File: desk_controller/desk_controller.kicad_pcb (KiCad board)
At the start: 2 copper layers, 92.8 x 125.7 mm, 56 parts, among them J2 UART_passthrough, J3 SWD_header, SW2 STRIP_PWR_SW, SW3 PC_PWR_RST_SW, SW4 OS_SW, U1 BD95831MUV, U2 PC817, U3 AP2112K-3.3, U4 TRS3243ECRHBR, U5 ISO7341FC, U6 STM32F030K6T6, U7 PC817

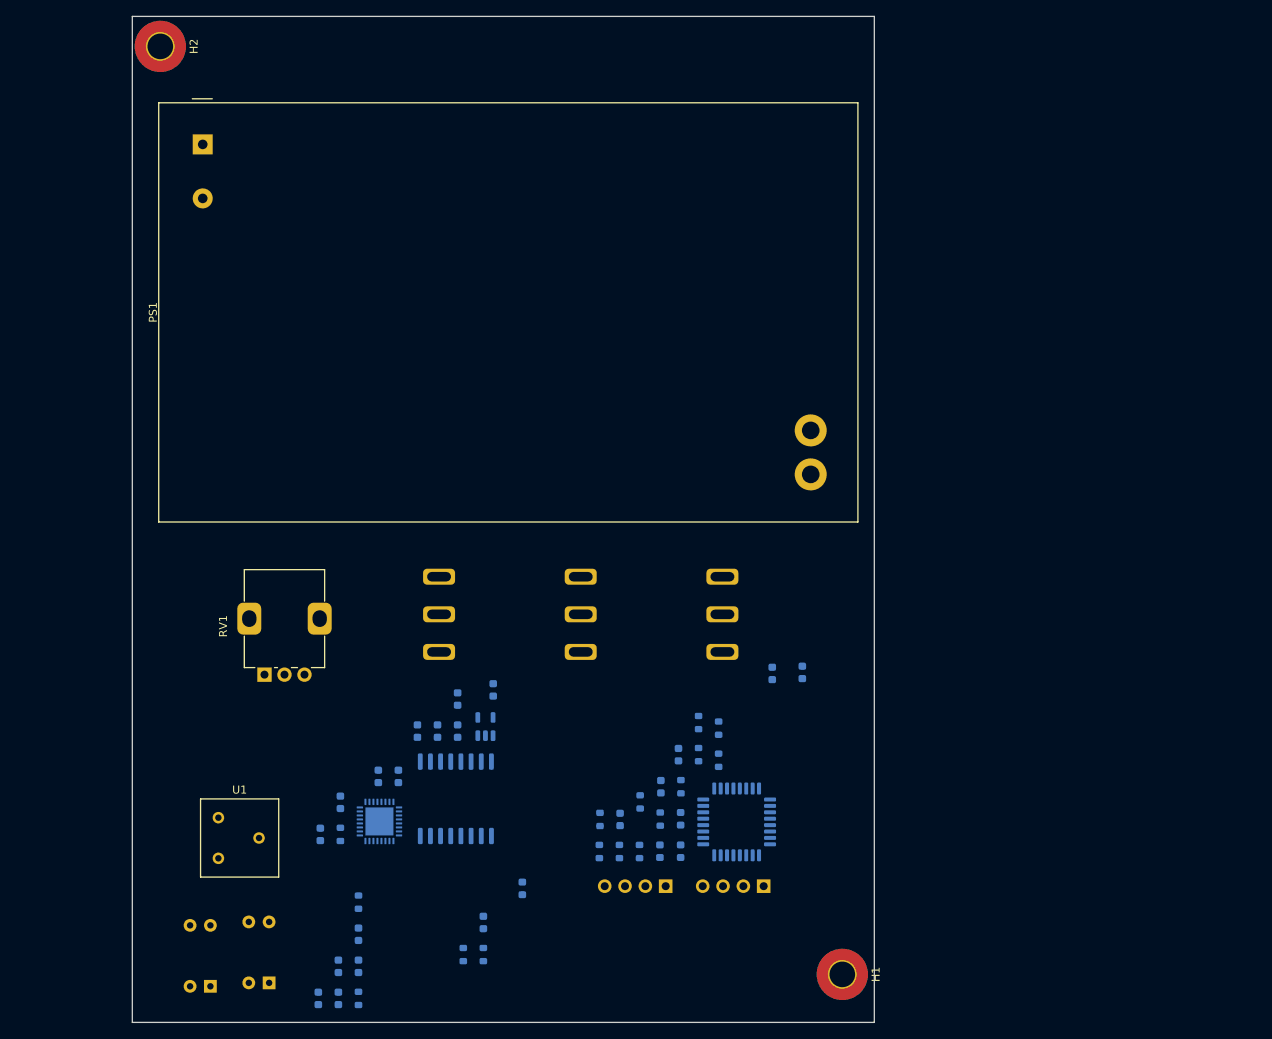
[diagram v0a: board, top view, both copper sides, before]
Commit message: Removed acdc brick
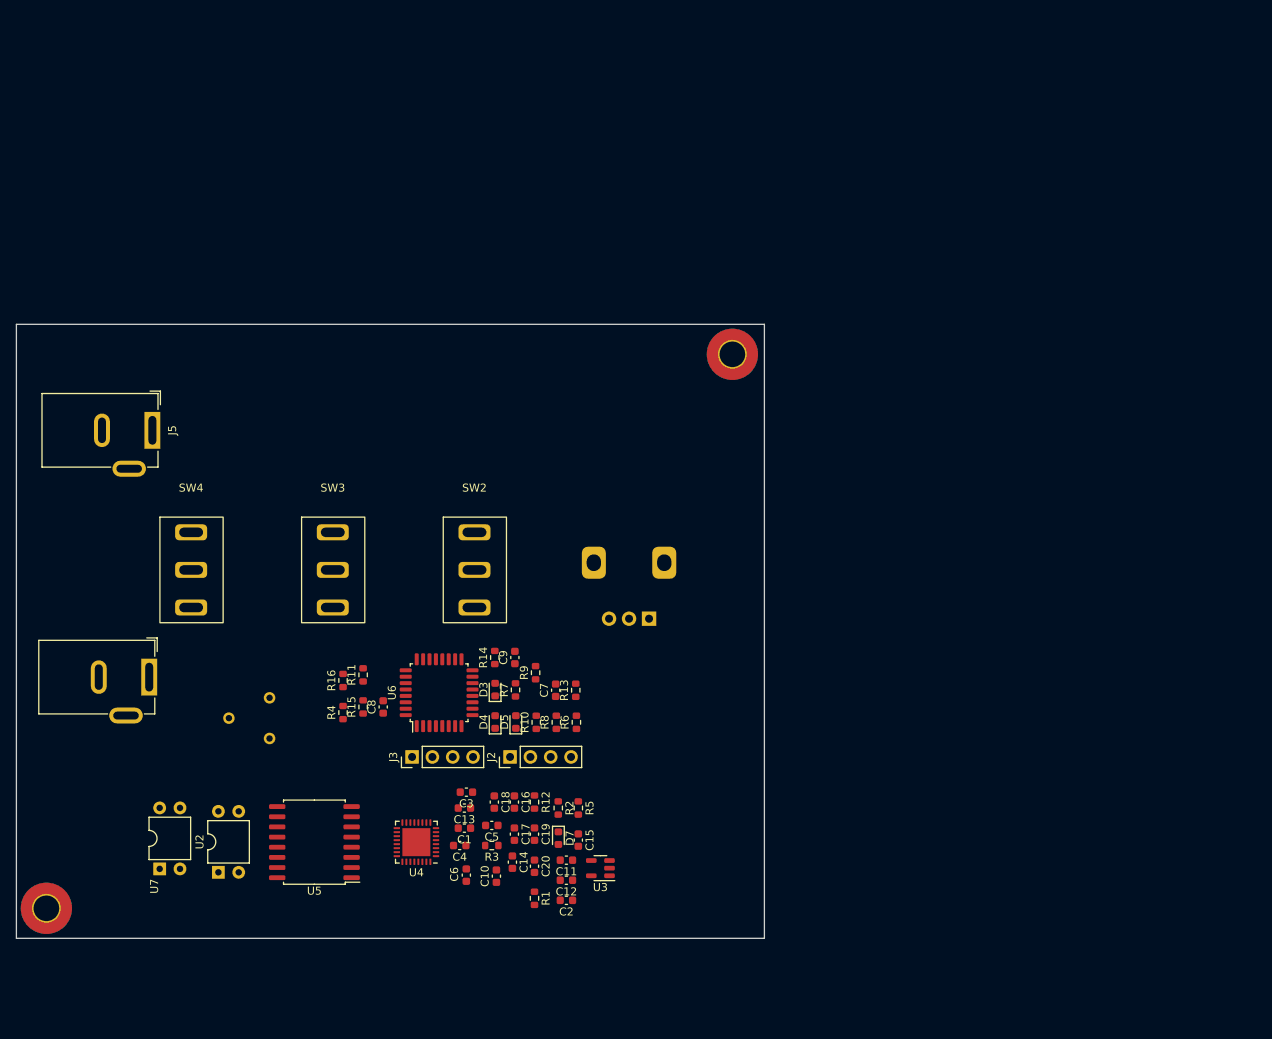
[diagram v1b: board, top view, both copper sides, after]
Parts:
- removed PS1: IRM-60-12, Converter_ACDC:Converter_ACDC_MeanWell_IRM-60-xx_THT
- added J4: Barrel_Jack_MountingPin, Connector_BarrelJack:BarrelJack_GCT_DCJ200-10-A_Horizontal, F.Cu at (105.8, 87.8)
- added J5: Barrel_Jack_MountingPin, Connector_BarrelJack:BarrelJack_GCT_DCJ200-10-A_Horizontal, F.Cu at (106.2, 57.0)
- C1, C10, C11, C12, C13, C14, C15, C16, C17, C18, C19, C2, C20, C3, C4, C5, C6, C7, C8, C9, D3, D4, D5, D7, J2, J3, R1, R10, R11, R12, R13, R14, R15, R16, R2, R3, R4, R5, R6, R7, R8, R9, SW2, SW3, SW4, U2, U3, U4, U5, U6, U7: moved to F.Cu
- RV1, U1: moved to B.Cu
- moved H1 99.8 mm to (93.0, 116.8)
- moved H2 81.2 mm to (178.8, 47.5)
- moved SW4 66.6 mm to (111.1, 74.5), turned to 0 degrees
- moved C6 49.1 mm to (145.5, 112.6)
- moved RV1 48.6 mm to (168.3, 80.5)
- moved R16 47.3 mm to (130.1, 88.3)
- moved R4 47.3 mm to (130.1, 92.3)
- moved J3 46.8 mm to (138.7, 97.8)
- moved C10 42.8 mm to (149.2, 112.7)
- moved R15 42.4 mm to (132.6, 91.6)
- moved R11 42.4 mm to (132.6, 87.6)
- moved U6 40.5 mm to (142.1, 89.8)
- moved C8 37.4 mm to (135.1, 91.6)
- moved C18 33.0 mm to (149.0, 103.5), turned to -90 degrees
- moved C16 33.0 mm to (151.5, 103.5), turned to -90 degrees
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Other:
- board size 92.8 x 125.7 mm -> 93.5 x 76.8 mm

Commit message: Much progress in sch and brd
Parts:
- removed C20: 22u, Capacitor_SMD:C_0603_1608Metric
- removed J2: UART_passthrough, Connector_PinHeader_2.54mm:PinHeader_1x04_P2.54mm_Vertical
- removed R12: 3k3, Resistor_SMD:R_0603_1608Metric
- removed R16: 1k, Resistor_SMD:R_0603_1608Metric
- removed RV1: STRIP_BRIGTH, Potentiometer_THT:Potentiometer_Alps_RK09K_Single_Vertical
- added D1: D_Schottky, Diode_SMD:D_0805_2012Metric, B.Cu at (238.9, 75.5)
- added D2: D_Schottky, Diode_SMD:D_0805_2012Metric, B.Cu at (238.9, 77.6)
- added D6: RED, LED_SMD:LED_0603_1608Metric, B.Cu at (199.2, 86.8)
- added J1: RJ45, Connector_RJ:RJ45_Ninigi_GE, F.Cu at (216.5, 85.3)
- added L1: 4u7, BWVS005050404R7M00:BWVS005050404R7M00, B.Cu at (198.5, 90.5)
- added Q1: RQ3E110AJ, SOTFL65P330X80-8N:SOTFL65P330X80-8N, B.Cu at (156.4, 51.5)
- added SW1: SW_Push_Open_Dual, SKRPACE010:SW_SKRPACE010, B.Cu at (188.6, 60.4)
- C1, C10, C11, C12, C13, C14, C15, C19, C2, C3, C4, C5, C6, C7, C8, C9, D7, J3, R13, R14, R15, R3, R4, R6, R7, R8, U2, U3, U4, U5, U6, U7: moved to B.Cu
- C16: value 22n -> 100n; moved to B.Cu
- C17: value 10u -> 22n; moved to B.Cu
- C18: value 1n -> 22u; moved to B.Cu
- R1: value 4k7 -> 10k; moved to B.Cu
- R2: value 1k5 -> 3k7; moved to B.Cu
- R5: value 13k -> 1k; moved to B.Cu
- SW2: value STRIP_PWR_SW -> RotaryEncoder; footprint MTS-102-103:MTS-102-103 -> Rotary_Encoder:RotaryEncoder_Alps_EC12E_Vertical_H20mm
- U1: value BD95831MUV -> TS30042-M000QFNR; footprint Potentiometer_THT:Potentiometer_Bourns_3386F_Vertical -> Package_DFN_QFN:QFN-16-1EP_3x3mm_P0.5mm_EP1.75x1.75mm_ThermalVias
- moved U5 103.4 mm to (216.7, 57.9)
- moved U7 103.2 mm to (205.3, 79.9), turned to 0 degrees
- moved C1 101.4 mm to (238.7, 67.5), turned to 0 degrees
- moved C3 99.8 mm to (236.7, 61.8), turned to 0 degrees
- moved U2 98.7 mm to (204.9, 72.6), turned to 0 degrees
- moved U4 97.6 mm to (231.9, 78.0)
- moved R3 96.4 mm to (235.7, 67.5)
- moved C4 96.3 mm to (223.9, 54.2), turned to -90 degrees
- moved C2 96.1 mm to (239.4, 64.8), turned to 90 degrees
- moved SW3 92.7 mm to (221.4, 74.5)
- moved C14 89.9 mm to (232.4, 72.5), turned to 0 degrees
- moved U3 87.8 mm to (236.3, 64.6)
- moved C13 87.1 mm to (226.9, 74.0), turned to -90 degrees
- moved C12 85.6 mm to (232.4, 71.0), turned to 0 degrees
- moved SW4 82.3 mm to (193.4, 74.3)
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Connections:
- net GND2 renamed PC_GND
- C15 pad 1: +12V -> GND
- C15 pad 2: GND -> +12V
- C16 pad 2: Net-(C16-Pad2) -> +12V
- C17 pad 1: GND -> Net-(C17-Pad1)
- C17 pad 2: +12V -> Net-(C17-Pad2)
- C18 pad 1: Net-(C18-Pad1) -> GND
- C18 pad 2: Net-(C18-Pad2) -> +3V3
- C19 pad 2: +3.3V -> +3V3
- C5 pad 1: Net-(C5-Pad1) -> GND
- R1 pad 1: Net-(R1-Pad1) -> +3V3
- R1 pad 2: GND -> Net-(R1-Pad2)
- R2 pad 1: Net-(R1-Pad1) -> Net-(R1-Pad2)
- R2 pad 2: Net-(R2-Pad2) -> GND
- R5 pad 1: Net-(R2-Pad2) -> Net-(D6-Pad2)
- R5 pad 2: +3.3V -> +3V3
- U1 pad 1: +12V -> Net-(C17-Pad2)
- U1 pad 3: GND -> +12V
- U2 pad 4: /mcu/POWER+ -> POWER
- U4 pad 12: TTL_RX -> /rs232/TTL_RX
- U4 pad 15: TTL_RTS -> /rs232/TTL_RTS
- U4 pad 17: TTL_DTR -> /rs232/TTL_DTR
- U4 pad 18: TTL_TX -> /rs232/TTL_TX
- U5 pad 11: TTL_RX -> TTL_RX_ISO
- U5 pad 12: TTL_RTS -> TTL_RTS_ISO
- U5 pad 13: TTL_DTR -> TTL_DTR_ISO
- U5 pad 14: TTL_TX -> TTL_TX_ISO
- U5 pad 15: Net-(C5-Pad1) -> GND
- U5 pad 3: /rs232/232_TX -> /rs232/TTL_TX
- U5 pad 4: /rs232/232_DTR -> /rs232/TTL_DTR
- U5 pad 5: /rs232/232_RTS -> /rs232/TTL_RTS
- U5 pad 6: /rs232/232_RX -> /rs232/TTL_RX
- U5 pad 9: Net-(C5-Pad1) -> GND
- U6 pad 10: unconnected-(U6-Pad10) -> TTL_TX_ISO
- U6 pad 11: unconnected-(U6-Pad11) -> TTL_DTR_ISO
- U6 pad 12: unconnected-(U6-Pad12) -> TTL_RTS_ISO
- U6 pad 13: unconnected-(U6-Pad13) -> TTL_RX_ISO
- U7 pad 4: /mcu/RESET+ -> RESET
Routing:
- net /rs232/232_VUR: track 0.00 -> 5.57 mm
- net GND1: track 0.00 -> 1.22 mm, vias 0 -> 1
- added copper zone on F.Cu, net GND
- added copper zone on F.Cu, net GND1
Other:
- board size 93.5 x 76.8 mm -> 94.9 x 51.6 mm
- board text added: "LINUX"
- board text added: "PWR"
- board text added: "RST"
- board text added: "WIN"

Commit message: moved to kicad 7, sch work
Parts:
- removed C10: 10u, Capacitor_SMD:C_0603_1608Metric
- removed C19: 22u, Capacitor_SMD:C_0603_1608Metric
- removed C6: 1u, Capacitor_SMD:C_0603_1608Metric
- removed C7, C8, C9: 100n, Capacitor_SMD:C_0603_1608Metric
- removed D4, D5, D6, D7: RED, LED_SMD:LED_0603_1608Metric
- removed L1: 4u7, BWVS005050404R7M00:BWVS005050404R7M00
- removed R10, R11, R13, R9: 3k3, Resistor_SMD:R_0603_1608Metric
- removed R2: 3k7, Resistor_SMD:R_0603_1608Metric
- removed R4: 22k, Resistor_SMD:R_0603_1608Metric
- removed R5: 1k, Resistor_SMD:R_0603_1608Metric
- removed SW1: SW_Push_Open_Dual, SKRPACE010:SW_SKRPACE010
- removed U3: AP2112K-3.3, Package_TO_SOT_SMD:SOT-23-5
- removed U6: STM32F030K6T6, Package_QFP:LQFP-32_7x7mm_P0.8mm
- added C20: 4u7, Capacitor_SMD:C_0603_1608Metric, B.Cu at (203.7, 51.5)
- added J6: debug_uart, Connector_PinHeader_2.54mm:PinHeader_1x03_P2.54mm_Vertical, F.Cu at (179.2, 68.9)
- added RV1: R_Potentiometer, Potentiometer_THT:Potentiometer_Alps_RK09L_Single_Vertical, F.Cu at (163.8, 71.6)
- added VR1: UA78M33CKVURG3, Library:TO229P990X252-3N, F.Cu at (153.3, 61.8)
- added VR2: UA78M33CKVURG3, Library:TO229P990X252-3N, B.Cu at (234.3, 91.3)
- C15: value 10u -> C
- C16: value 100n -> C
- C17: value 22n -> 100n
- C18: value 22u -> 100n
- C2: value 1u -> 330n
- C3: value 1u -> 100n
- D3: value GREEN -> RED; moved to B.Cu
- J1: footprint Connector_RJ:RJ45_Ninigi_GE -> RJ45_midplane:RJ45_midplane
- R1: value 10k -> 3k3
- R3: value R -> 1k
- SW2: value RotaryEncoder -> SW_Push_Open_Dual; footprint Rotary_Encoder:RotaryEncoder_Alps_EC12E_Vertical_H20mm -> SKRPACE010:SW_SKRPACE010; moved to B.Cu
- U1: value TS30042-M000QFNR -> STM32C011F4Ux; footprint Package_DFN_QFN:QFN-16-1EP_3x3mm_P0.5mm_EP1.75x1.75mm_ThermalVias -> Package_DFN_QFN:ST_UFQFPN-20_3x3mm_P0.5mm
- moved D3 55.4 mm to (203.4, 55.5), turned to -90 degrees
- moved SW2 45.8 mm to (199.8, 57.1), turned to -90 degrees
- moved R1 40.4 mm to (206.2, 51.5)
- moved C18 38.8 mm to (201.2, 51.5)
- moved C17 36.1 mm to (198.7, 51.5), turned to -90 degrees
- moved U1 33.4 mm to (195.2, 57.1)
- moved Q1 16.5 mm to (171.7, 57.8), turned to 180 degrees
- moved R8 16.3 mm to (172.4, 61.5), turned to 180 degrees
- moved J1 7.05 mm to (219.9, 91.5)
- moved J4 6.01 mm to (165.1, 63.2), turned to 180 degrees
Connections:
- net POWER renamed PC_POWER
- net RESET renamed PC_RESET
- C11 pad 1: /rs232/232_VCC -> /rs232/232_VCC_3V3
- C15 pad 1: GND -> +3.3V
- C15 pad 2: +12V -> GND
- C16 pad 1: GND -> +12V
- C16 pad 2: +12V -> GND
- C17 pad 1: Net-(C17-Pad1) -> +3V3
- C17 pad 2: Net-(C17-Pad2) -> GND
- C18 pad 1: GND -> /mcu/NRST
- C18 pad 2: +3V3 -> GND
- C3 pad 1: /rs232/232_VCC -> /rs232/232_VCC_3V3
- C4 pad 1: /rs232/232_VCC -> /rs232/232_VCC_3V3
- D3 pad 2: Net-(D3-Pad2) -> Net-(D3-A)
- R1 pad 1: +3V3 -> Net-(U1-PB7)
- R1 pad 2: Net-(R1-Pad2) -> Net-(D3-A)
- U1 pad 1: Net-(C17-Pad2) -> unconnected-(U1-PC15-Pad1)
- U1 pad 10: Net-(C17-Pad1) -> unconnected-(U1-PA5-Pad10)
- U1 pad 11: +12V -> unconnected-(U1-PA6-Pad11)
- U1 pad 12: Net-(C17-Pad2) -> unconnected-(U1-PA7-Pad12)
- U1 pad 13: Net-(C17-Pad2) -> unconnected-(U1-PA8-Pad13)
- U1 pad 14: GND -> TTL_TX_ISO
- U1 pad 15: GND -> TTL_RX_ISO
- U1 pad 16: Net-(C17-Pad2) -> unconnected-(U1-PA13-Pad16)
- U1 pad 17: GND -> /mcu/BOOT0
- U1 pad 2: +12V -> +3V3
- U1 pad 3: +12V -> GND
- U1 pad 4: GND -> /mcu/NRST
- U1 pad 5: Net-(R1-Pad2) -> TX
- U1 pad 6: unconnected-(U1-Pad6) -> RX
- U4 pad 21: /rs232/232_VCC -> Net-(JP1-B)
- U4 pad 22: GND1 -> Net-(JP2-A)
- U4 pad 26: /rs232/232_VCC -> /rs232/232_VCC_3V3
- U5 pad 1: /rs232/232_VCC -> /rs232/232_VCC_3V3
- U5 pad 7: /rs232/232_VCC -> /rs232/232_VCC_3V3
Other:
- outline, holes or cut-outs redrawn
